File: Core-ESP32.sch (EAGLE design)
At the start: 77 parts, among them Q1 BSS138, Q10 BSS138, Q11 BSS138, Q12 BSS138, Q13 BSS138, Q14 BSS138, Q15 BSS138, Q16 BSS138, Q17 BSS138, Q2 BSS138, Q3 BSS138, Q4 BSS138, Q5 BSS138, Q6 BSS138, Q7 BSS138, Q8 BSS138, Q9 BSS138

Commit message: SPCoast lbr footprint update
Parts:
- renumbered FID1 to FID-LR, FID2 to FID-UL
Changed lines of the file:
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@@
 <part name="3V1" library="supply1" deviceset="+3V3" device=""/>
 <part name="VCC15" library="supply1" deviceset="VCCIO" device=""/>
-<part name="FID1" library="SPCoast" deviceset="FIDUCIAL" device=""/>
-<part name="FID2" library="SPCoast" deviceset="FIDUCIAL" device=""/>
+<part name="FID-LR" library="SPCoast" deviceset="FIDUCIAL" device=""/>
+<part name="FID-UL" library="SPCoast" deviceset="FIDUCIAL" device=""/>
 <part name="LED1" library="SPCoast" deviceset="LED*" device="0603-LED" value="G"/>
 <part name="R35" library="SPCoast" deviceset="R*" device="0603-RES" value="2k2"/>
@@
 <instance part="CON1" gate="G$1" x="132.08" y="66.04" rot="R180"/>
 <instance part="VCC12" gate="G$1" x="114.3" y="60.96"/>
-<instance part="FID1" gate="FID1" x="243.84" y="48.26"/>
-<instance part="FID2" gate="FID1" x="243.84" y="55.88"/>
+<instance part="FID-LR" gate="FID1" x="243.84" y="48.26"/>
+<instance part="FID-UL" gate="FID1" x="243.84" y="55.88"/>
 <instance part="LED1" gate="LED" x="86.36" y="17.78"/>
 <instance part="R35" gate="R" x="86.36" y="27.94" rot="R90"/>

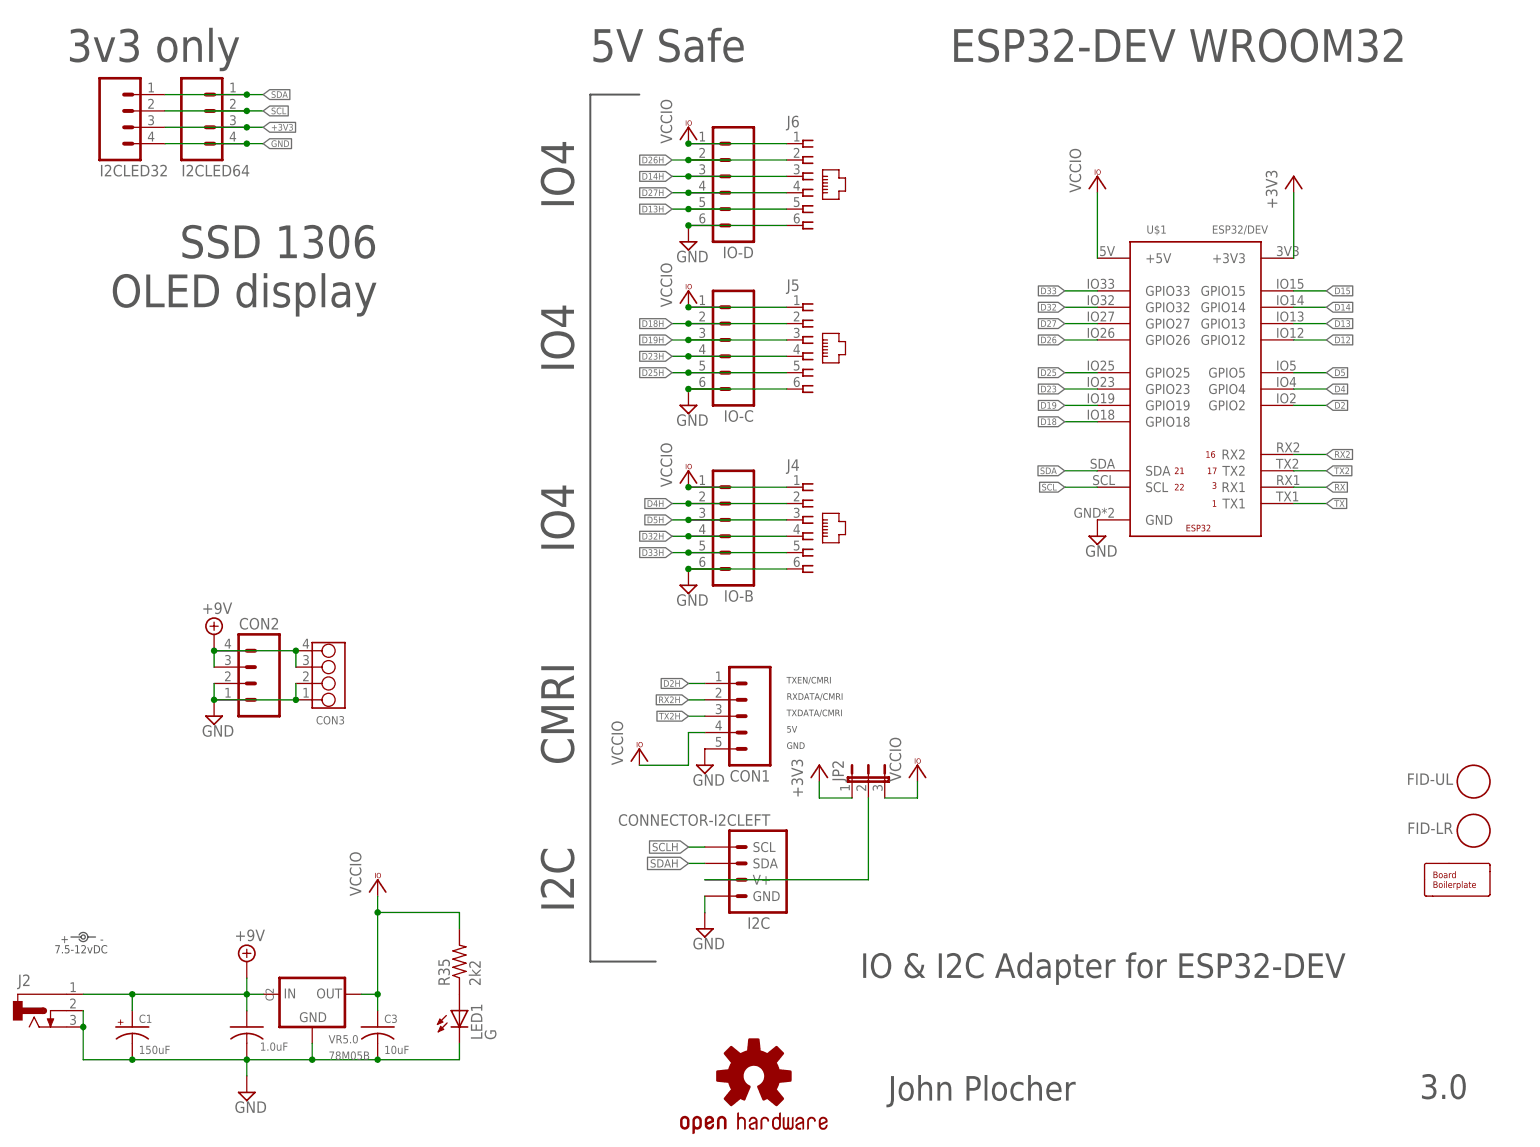
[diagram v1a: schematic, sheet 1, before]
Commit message: added values for connectors
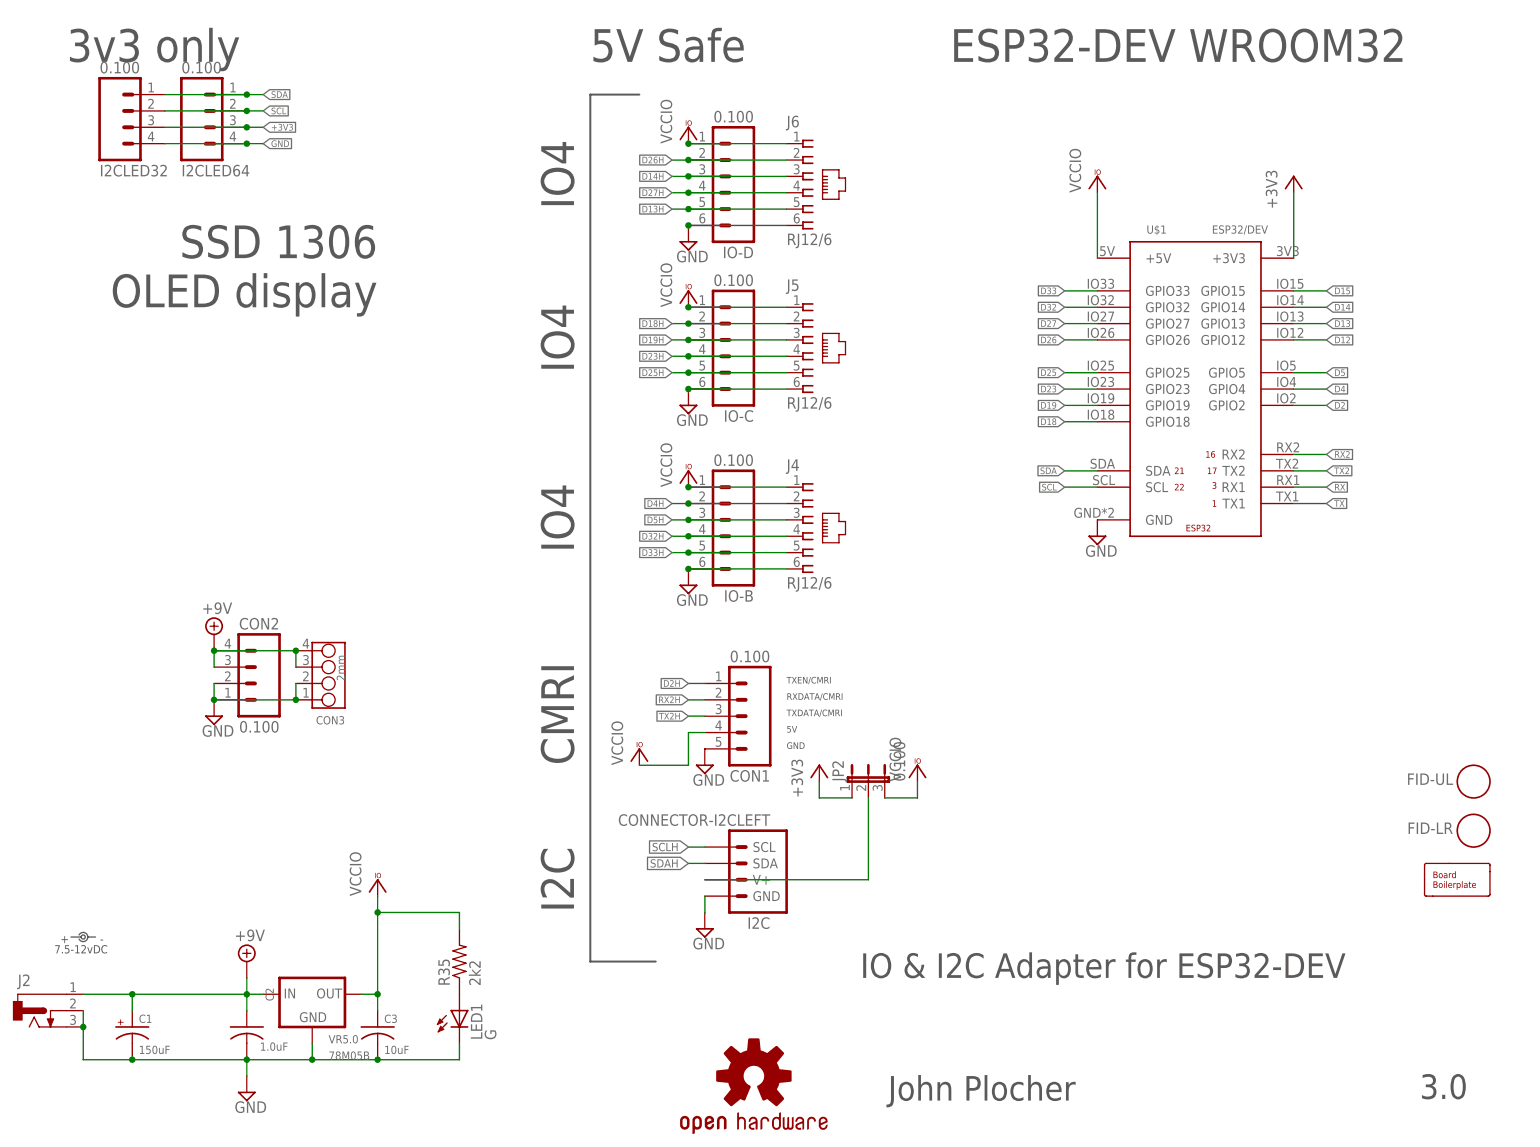
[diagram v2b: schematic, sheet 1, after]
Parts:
- CON1, CON2, I2CLED32, I2CLED64, IO-B, IO-C, IO-D, JP2: value (none) -> 0.100
- CON3: value (none) -> 2mm
- J4, J5, J6: value (none) -> RJ12/6
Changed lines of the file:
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@@
 <part name="VCC26" library="supply1" deviceset="VCCIO" device=""/>
 <part name="V4" library="supply2" deviceset="GND" device=""/>
-<part name="J4" library="SPCoast" deviceset="CONNECTOR-RJ25" device="-43860-2-MOLEX"/>
-<part name="IO-B" library="SPCoast" deviceset="CONNECTOR-M06" device="LOCK"/>
+<part name="J4" library="SPCoast" deviceset="CONNECTOR-RJ25" device="-43860-2-MOLEX" value="RJ12/6"/>
+<part name="IO-B" library="SPCoast" deviceset="CONNECTOR-M06" device="LOCK" value="0.100"/>
 <part name="V7" library="supply2" deviceset="GND" device=""/>
 <part name="VCC29" library="supply1" deviceset="VCCIO" device=""/>
-<part name="IO-C" library="SPCoast" deviceset="CONNECTOR-M06" device="LOCK"/>
-<part name="J5" library="SPCoast" deviceset="CONNECTOR-RJ25" device="-43860-2-MOLEX"/>
+<part name="IO-C" library="SPCoast" deviceset="CONNECTOR-M06" device="LOCK" value="0.100"/>
+<part name="J5" library="SPCoast" deviceset="CONNECTOR-RJ25" device="-43860-2-MOLEX" value="RJ12/6"/>
 <part name="VCC30" library="supply1" deviceset="VCCIO" device=""/>
 <part name="V8" library="supply2" deviceset="GND" device=""/>
-<part name="I2CLED32" library="SPCoast" deviceset="CONNECTOR-M04" device="LOCK"/>
-<part name="I2CLED64" library="SPCoast" deviceset="CONNECTOR-M04" device="LOCK"/>
-<part name="J6" library="SPCoast" deviceset="CONNECTOR-RJ25" device="-43860-2-MOLEX"/>
+<part name="I2CLED32" library="SPCoast" deviceset="CONNECTOR-M04" device="LOCK" value="0.100"/>
+<part name="I2CLED64" library="SPCoast" deviceset="CONNECTOR-M04" device="LOCK" value="0.100"/>
+<part name="J6" library="SPCoast" deviceset="CONNECTOR-RJ25" device="-43860-2-MOLEX" value="RJ12/6"/>
 <part name="VCC1" library="supply1" deviceset="VCCIO" device=""/>
 <part name="V3" library="supply2" deviceset="GND" device=""/>
@@
 <part name="3V7" library="supply1" deviceset="+3V3" device=""/>
 <part name="VCC4" library="supply1" deviceset="VCCIO" device=""/>
-<part name="IO-D" library="SPCoast" deviceset="CONNECTOR-M06" device="LOCK"/>
+<part name="IO-D" library="SPCoast" deviceset="CONNECTOR-M06" device="LOCK" value="0.100"/>
 <part name="Q15" library="SPCoast" deviceset="MOSFET-N-*-?" device="SOT23" technology="BSS138" value="BSS138"/>
 <part name="R1" library="SPCoast" deviceset="R*" device="0603-RES" value="10k"/>
@@
 <part name="3V11" library="supply1" deviceset="+3V3" device=""/>
 <part name="VCC10" library="supply1" deviceset="VCCIO" device=""/>
-<part name="CON1" library="SPCoast" deviceset="CONNECTOR-M05" device="LOCK"/>
+<part name="CON1" library="SPCoast" deviceset="CONNECTOR-M05" device="LOCK" value="0.100"/>
 <part name="VCC12" library="supply1" deviceset="VCCIO" device=""/>
 <part name="Q17" library="SPCoast" deviceset="MOSFET-N-*-?" device="SOT23" technology="BSS138" value="BSS138"/>
@@
 <part name="LED1" library="SPCoast" deviceset="LED*" device="0603-LED" value="G"/>
 <part name="R35" library="SPCoast" deviceset="R*" device="0603-RES" value="2k2"/>
-<part name="CON2" library="SPCoast" deviceset="CONNECTOR-M04" device="LOCK"/>
-<part name="CON3" library="SPCoast" deviceset="CONNECTOR-GROVE-4P-2.0" device="-3470130P1"/>
+<part name="CON2" library="SPCoast" deviceset="CONNECTOR-M04" device="LOCK" value="0.100"/>
+<part name="CON3" library="SPCoast" deviceset="CONNECTOR-GROVE-4P-2.0" device="-3470130P1" value="2mm"/>
 <part name="SUPPLY3" library="supply2" deviceset="+9V" device=""/>
 <part name="V6" library="supply2" deviceset="GND" device=""/>
 <part name="VCC17" library="supply1" deviceset="VCCIO" device=""/>
-<part name="JP2" library="SPCoast" deviceset="JUMPER-3" device="PTH-LOCK"/>
+<part name="JP2" library="SPCoast" deviceset="JUMPER-3" device="PTH-LOCK" value="0.100"/>
 <part name="3V13" library="supply1" deviceset="+3V3" device=""/>
 </parts>

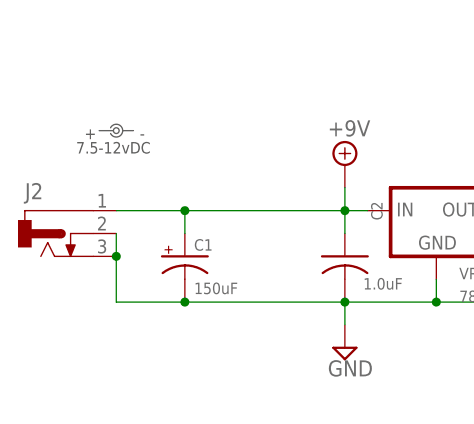
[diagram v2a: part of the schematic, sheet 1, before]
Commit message: added values for connectors
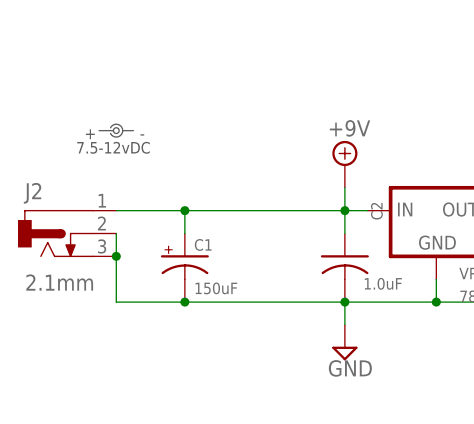
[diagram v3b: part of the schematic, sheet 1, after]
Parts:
- J2: value (none) -> 2.1mm
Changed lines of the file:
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@@
 <part name="I2C" library="SPCoast" deviceset="CONNECTOR-I2C" device="LEFT" value="CONNECTOR-I2CLEFT"/>
 <part name="V1" library="supply2" deviceset="GND" device=""/>
-<part name="J2" library="SPCoast" deviceset="CONNECTOR-DC-POWER" device="-RA"/>
+<part name="J2" library="SPCoast" deviceset="CONNECTOR-DC-POWER" device="-RA" value="2.1mm"/>
 <part name="LABEL1" library="SPCoast" deviceset="DOC-POWER_LABEL" device="" value="7.5-12vDC"/>
 <part name="BOARD" library="SPCoast" deviceset="BOARD" device="80X100-IOB" value="BOARD80X150"/>

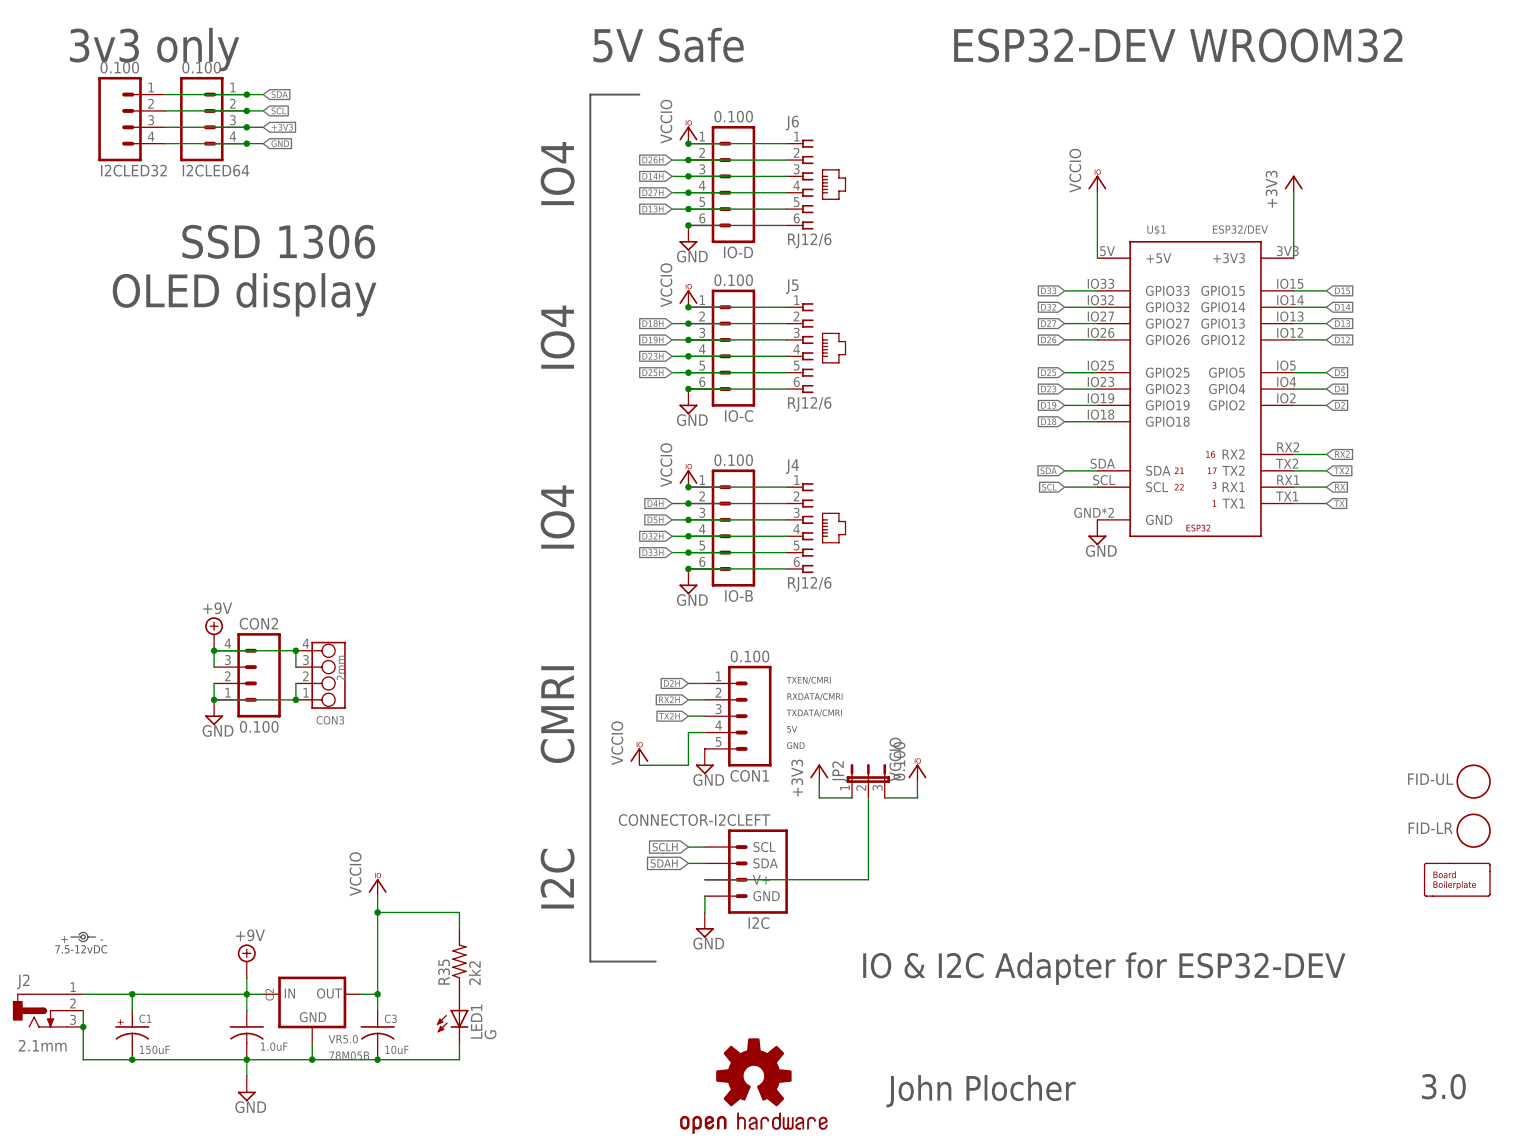
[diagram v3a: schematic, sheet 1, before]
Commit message: normalized values
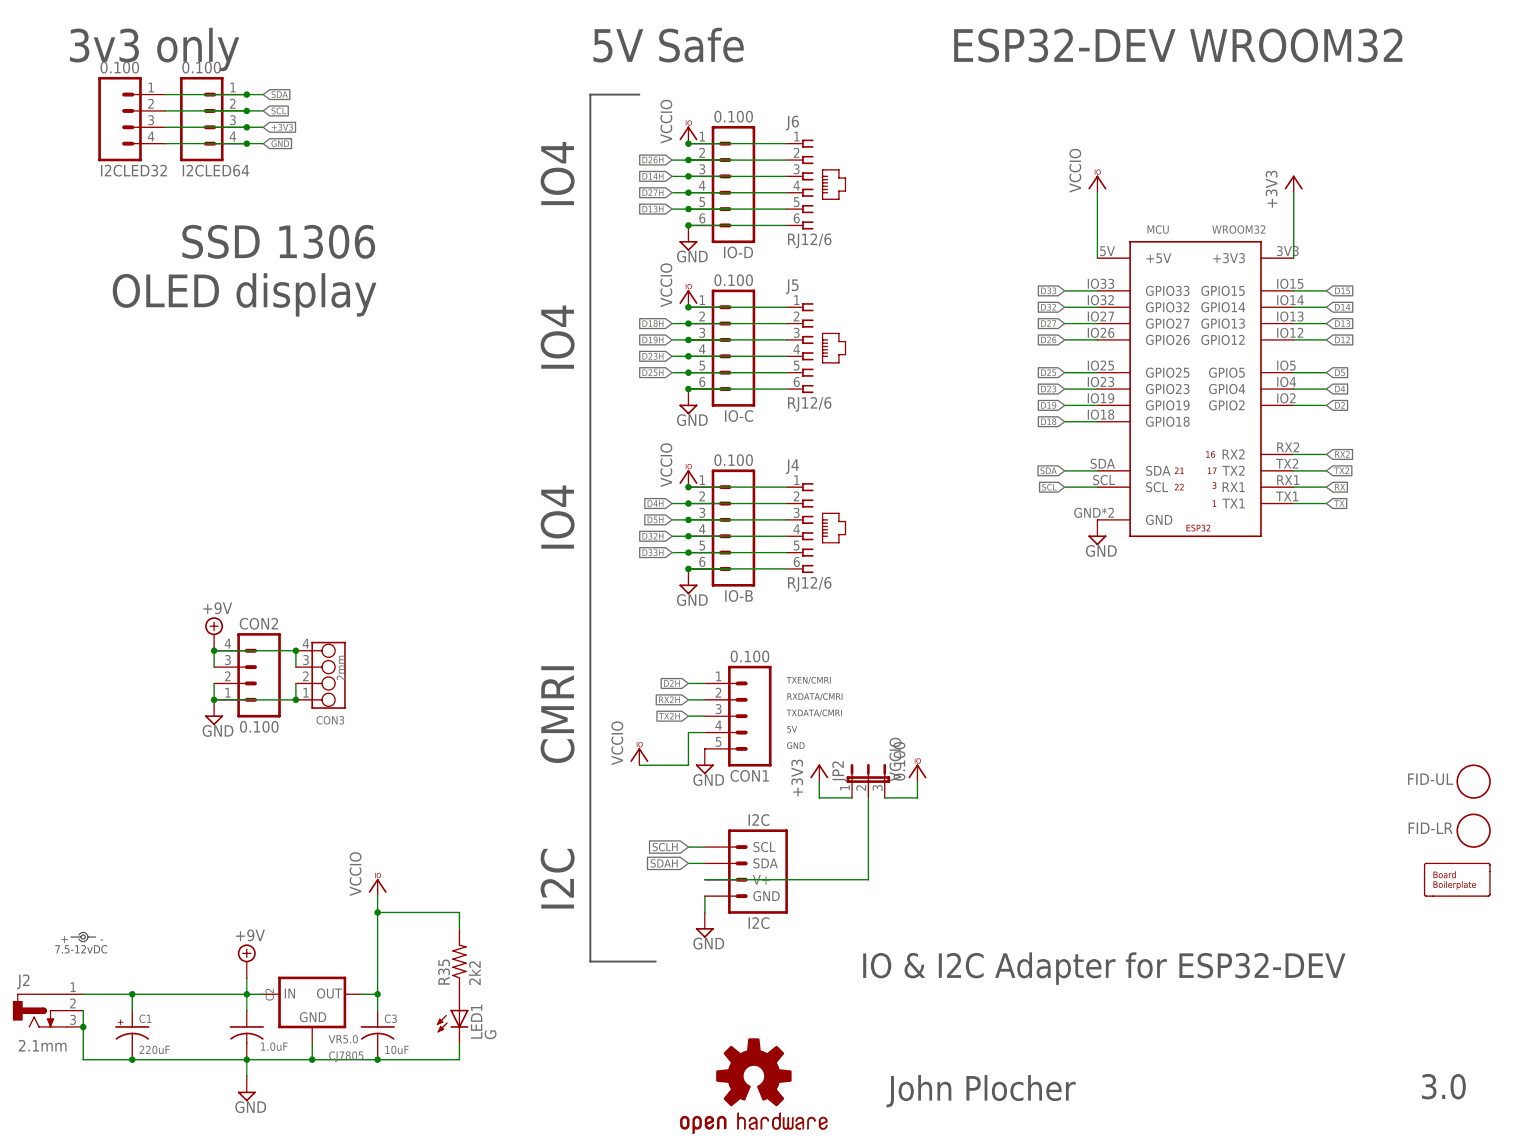
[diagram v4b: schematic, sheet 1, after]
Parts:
- BOARD: value BOARD80X150 -> BOARD
- C1: value 150uF -> 220uF
- I2C: value CONNECTOR-I2CLEFT -> I2C
- MCU: value ESP32/DEV -> WROOM32
- OSHW1: value OSHW-LOGOL -> OSHW
- VR5.0: value 78M05B -> CJ7805
- renumbered U$1 to MCU
